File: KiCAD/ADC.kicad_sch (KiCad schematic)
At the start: 32 parts, among them U2 MAX11059, U3 MAX11059

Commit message: Finished routing
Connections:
- net RDC1: now reaches C6.1, C7.1, C8.1, C9.1, U2.26 (RDC_SENSE), U2.27 (RDC), U2.33 (RDC), U2.40 (RDC), U2.48 (RDC), U2.54 (RDC), U2.55 (RDC_SENSE)
- net RDC2: now reaches C10.1, C11.1, C12.1, C13.1, U3.26 (RDC_SENSE), U3.27 (RDC), U3.33 (RDC), U3.40 (RDC), U3.48 (RDC), U3.54 (RDC), U3.55 (RDC_SENSE)
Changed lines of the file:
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@@
+		)
+	)
+	(label "RDC1"
+		(at 172.72 71.12 0)
+		(effects
+			(font
+				(size 1.27 1.27)
+			)
+			(justify left bottom)
 		)
 	)
@@
 		(effects
 			(font
+				(size 1.27 1.27)
+			)
+			(justify left bottom)
+		)
+	)
+	(label "RDC2"
+		(at 350.52 71.12 0)
+		(effects
+			(font

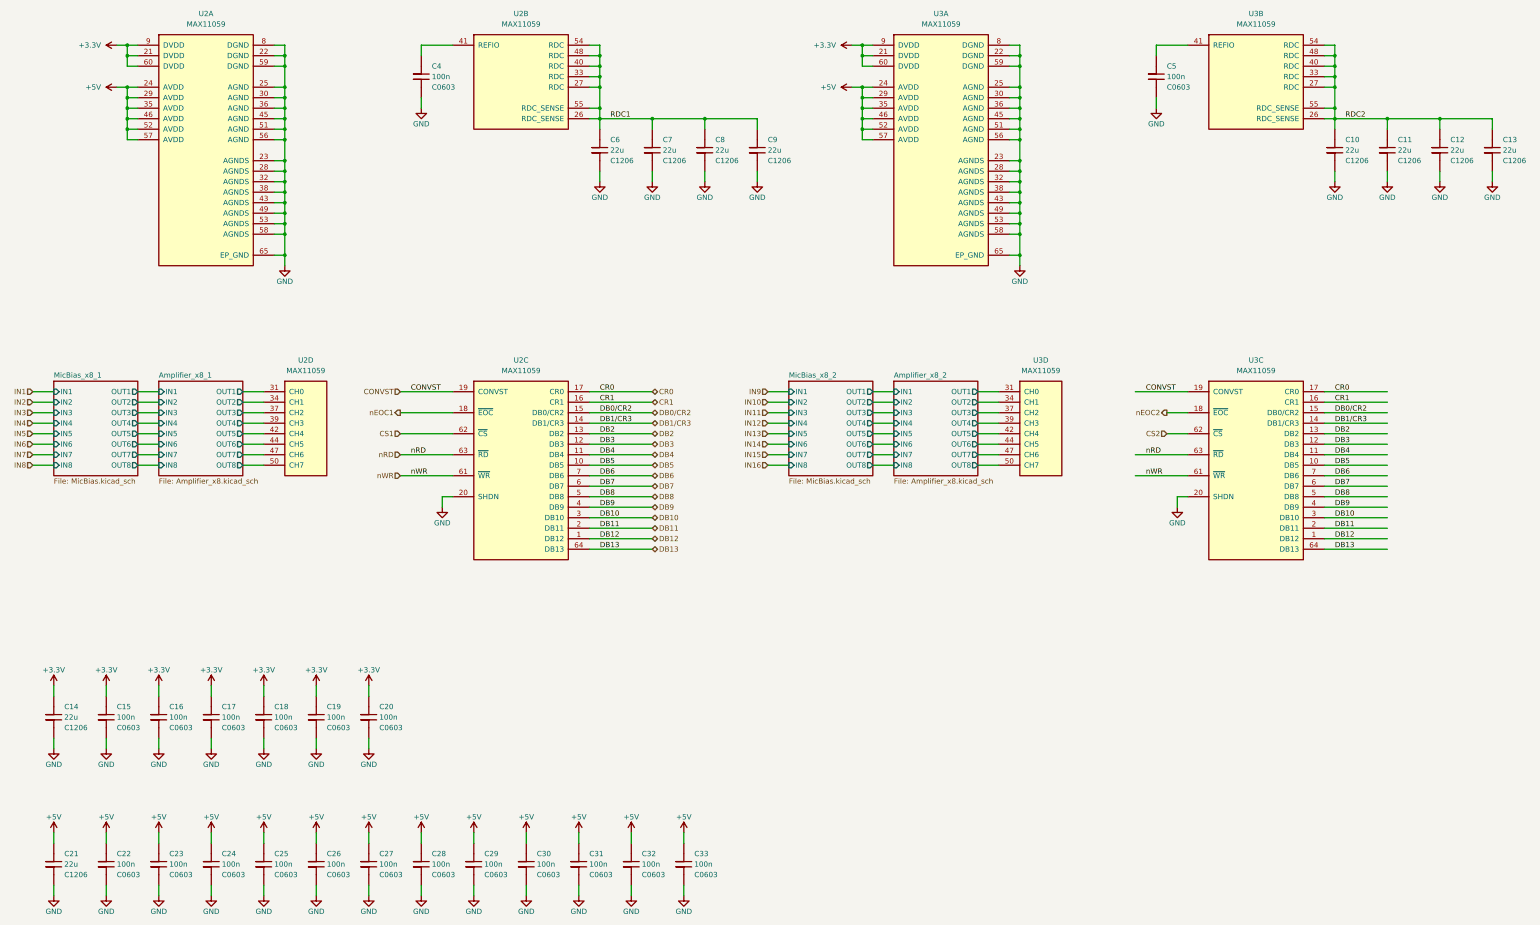
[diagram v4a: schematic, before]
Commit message: Moved the microphone RL to per-channel instead of per-mic
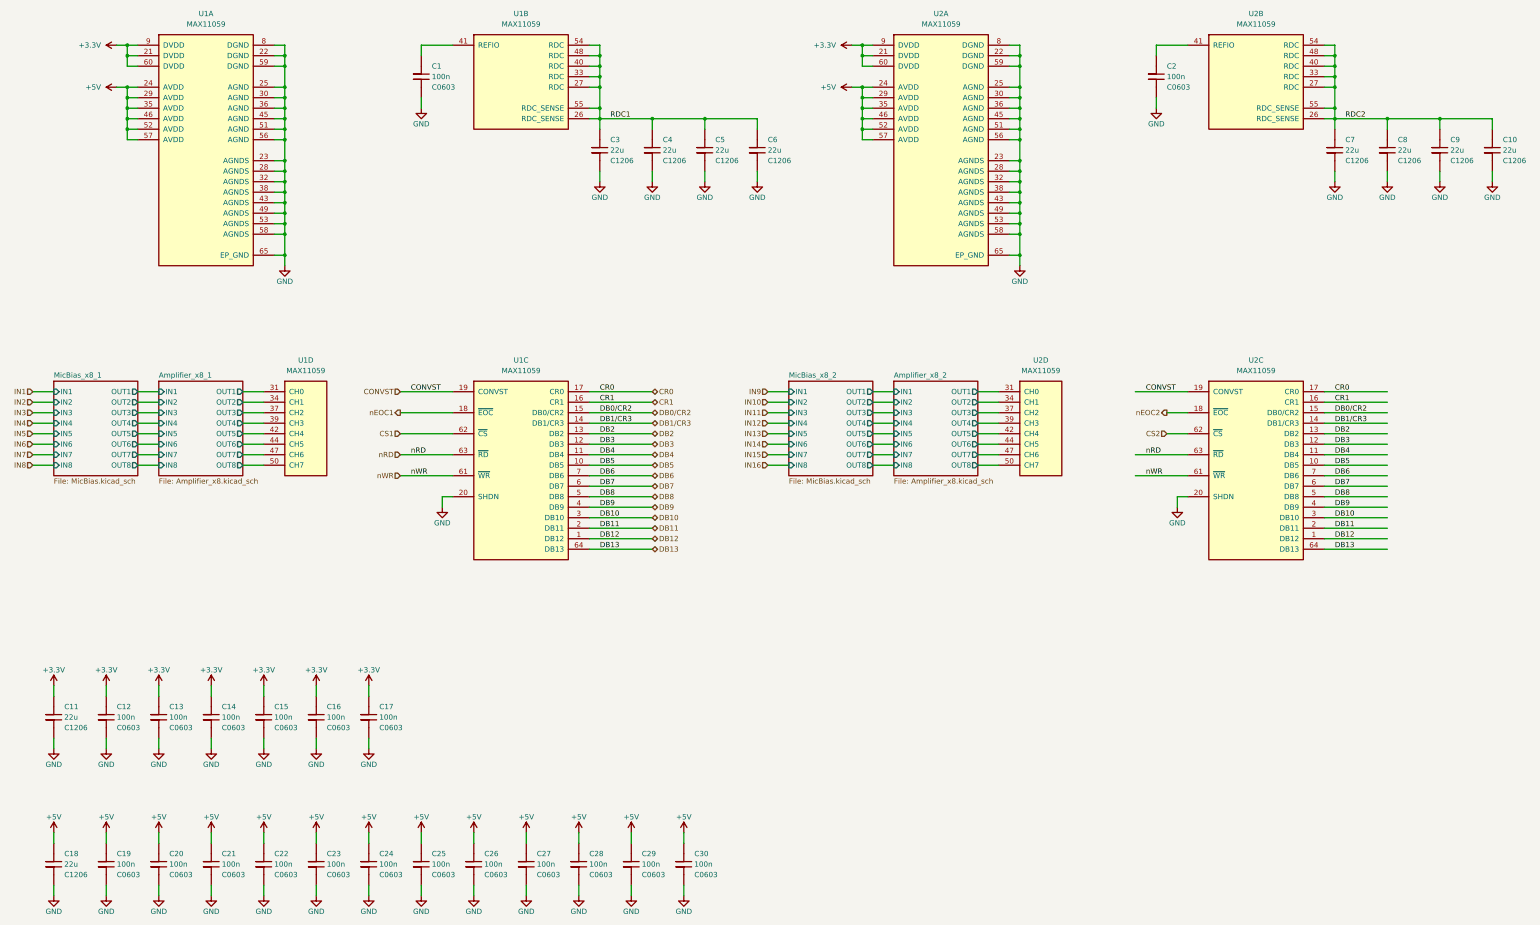
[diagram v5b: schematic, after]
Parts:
- renumbered C4 to C1, C13 to C10, C14 to C11, C15 to C12, C16 to C13, C17 to C14, C18 to C15, C19 to C16, C20 to C17, C21 to C18, C22 to C19, C5 to C2, C23 to C20, C24 to C21, C25 to C22, C26 to C23, C27 to C24, C28 to C25, C29 to C26, C30 to C27, C31 to C28, C32 to C29, C6 to C3, C33 to C30, C7 to C4, C8 to C5, C9 to C6, C10 to C7, C11 to C8, C12 to C9, U2 to U1, U3 to U2

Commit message: Added title block and version text
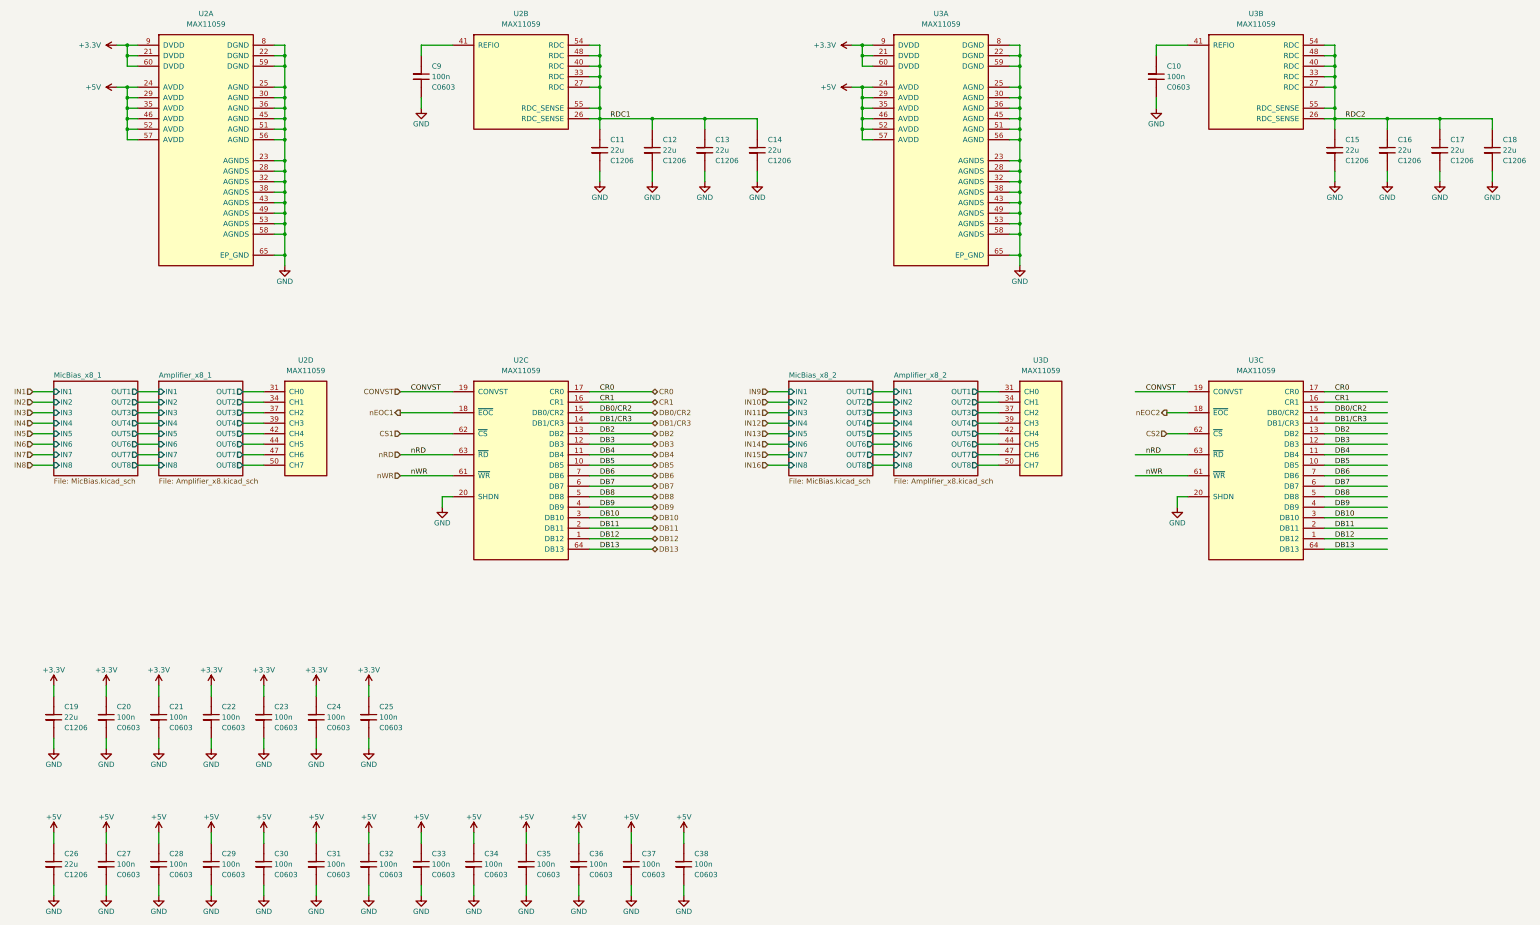
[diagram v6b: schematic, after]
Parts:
- renumbered C2 to C10, C3 to C11, C4 to C12, C5 to C13, C6 to C14, C7 to C15, C8 to C16, C9 to C17, C10 to C18, C11 to C19, C12 to C20, C13 to C21, C14 to C22, C15 to C23, C16 to C24, C17 to C25, C18 to C26, C19 to C27, C20 to C28, C21 to C29, C22 to C30, C23 to C31, C24 to C32, C25 to C33, C26 to C34, C27 to C35, C28 to C36, C29 to C37, C30 to C38, C1 to C9, U1 to U2, U2 to U3
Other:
- company: (none) -> University of Cape Town
- title: (none) -> Analogue to Digital Converter

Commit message: Regenerated CAM output
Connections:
- net CS1 renamed nCS1
- net CS2 renamed nCS2
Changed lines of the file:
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@@
 		(rev "v1.0")
 		(company "University of Cape Town")
+		(comment 1 "Radar Remote Sensing Group")
+		(comment 2 "Radar Masters")
 	)
 	(junction
@@
 		)
 	)
-	(hierarchical_label "CS2"
+	(hierarchical_label "nCS2"
 		(shape input)
 		(at 307.34 147.32 180)
@@
 		)
 	)
-	(hierarchical_label "CS1"
+	(hierarchical_label "nCS1"
 		(shape input)
 		(at 121.92 147.32 180)
